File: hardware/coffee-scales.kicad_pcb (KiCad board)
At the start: 2 copper layers, 121.9 x 50.8 mm, 10 parts, among them J1 Conn_01x04, SW1 SW_Push, U1 Adafruit_Feather_328P, U2 HX711_Breakout, U3 4DIGIT_7SEG, U4 4DIGIT_7SEG

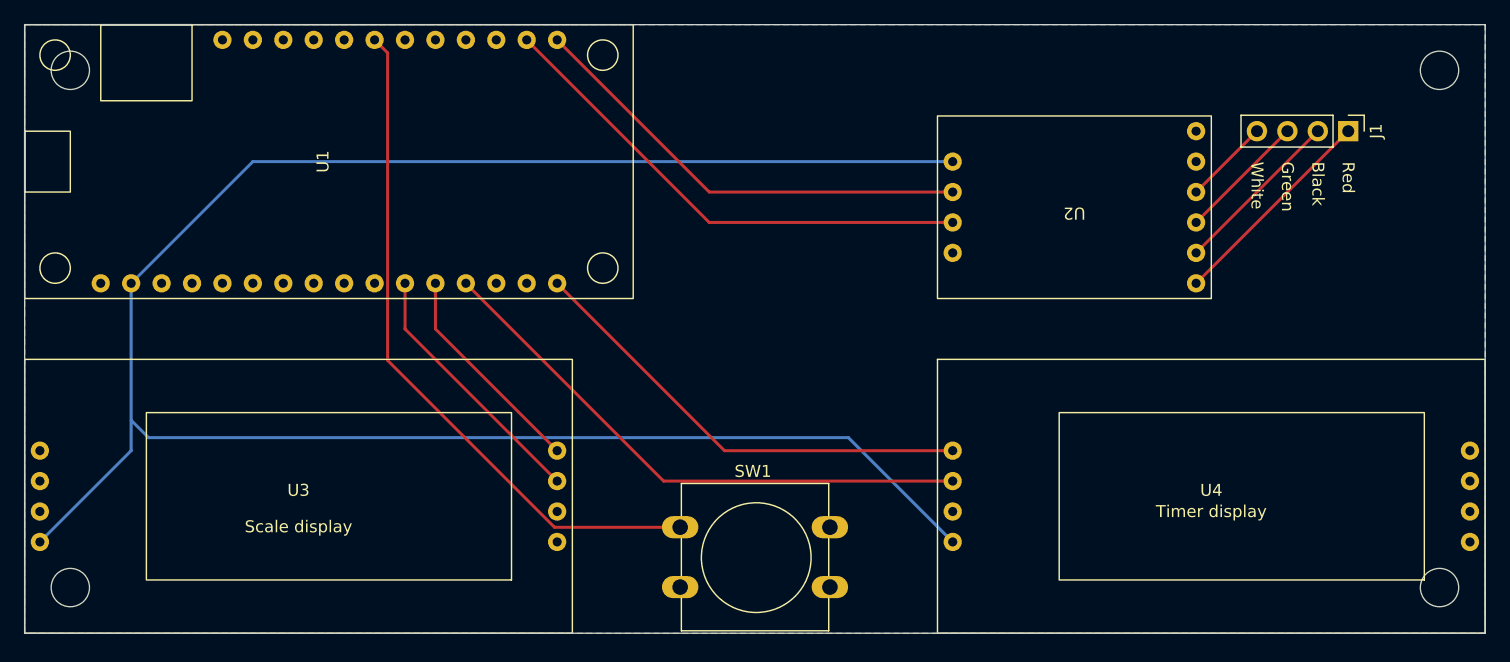
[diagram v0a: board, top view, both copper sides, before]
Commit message: Wire button and HX711 DT to interrupt pins
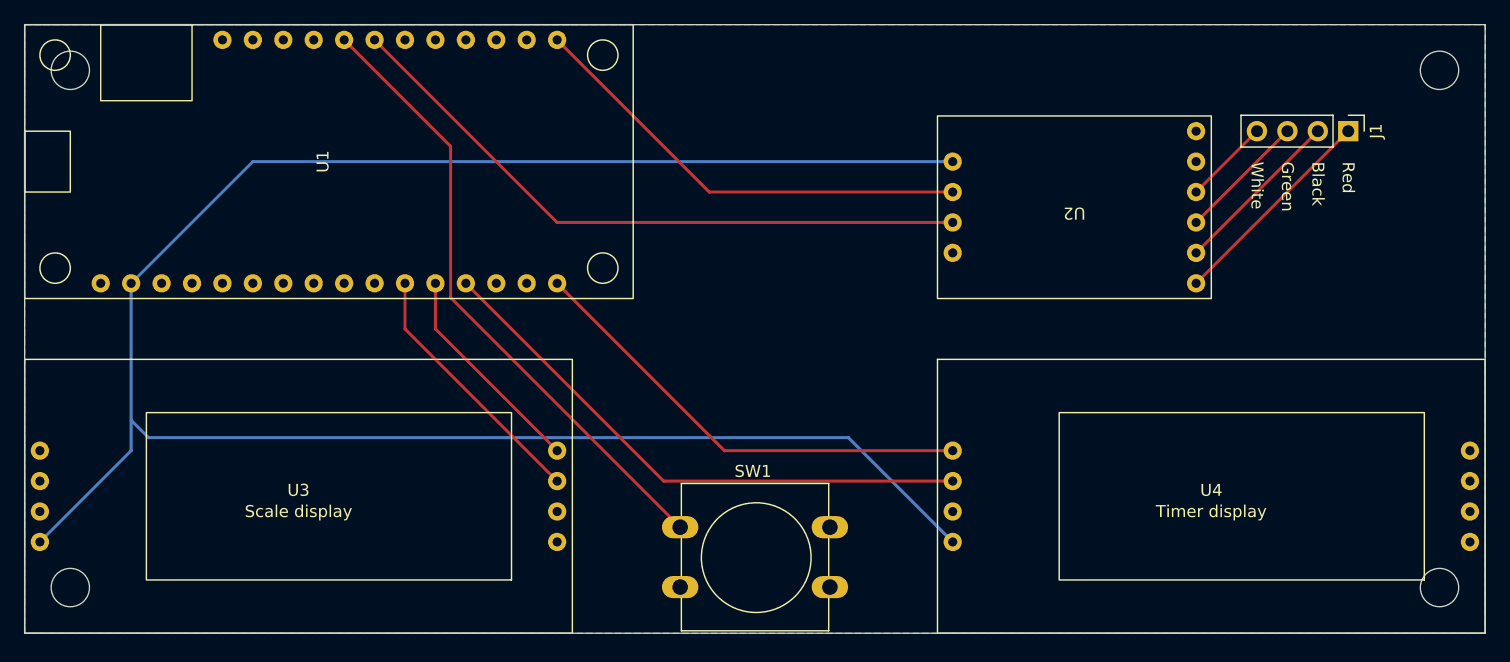
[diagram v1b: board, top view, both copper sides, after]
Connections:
- SW1 pad 1: Net-(U1-Pad22) -> Net-(SW1-Pad1)
- U1 pad 21: unconnected-(U1-Pad21) -> Net-(SW1-Pad1)
- U1 pad 27: Net-(U2-Pad8) -> unconnected-(U1-Pad27)
- U2 pad 8: Net-(U2-Pad8) -> Net-(U1-Pad22)
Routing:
- net Net-(SW1-Pad1): track 0.00 -> 52.3 mm
- net Net-(U2-Pad8): track 41.9 -> 0.00 mm
- net Net-(U1-Pad22): track 57.4 -> 54.6 mm

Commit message: Big but pointless PCB update
* Rounded corners
* Components not so close to the edge
* HX711 data pin on interrupt
* Bigger vias/pads
* Square first pad
* Lots of stuff added to silkscreen

But my gut feeling is the next PCB I have made will be without
all the breakouts anyway.
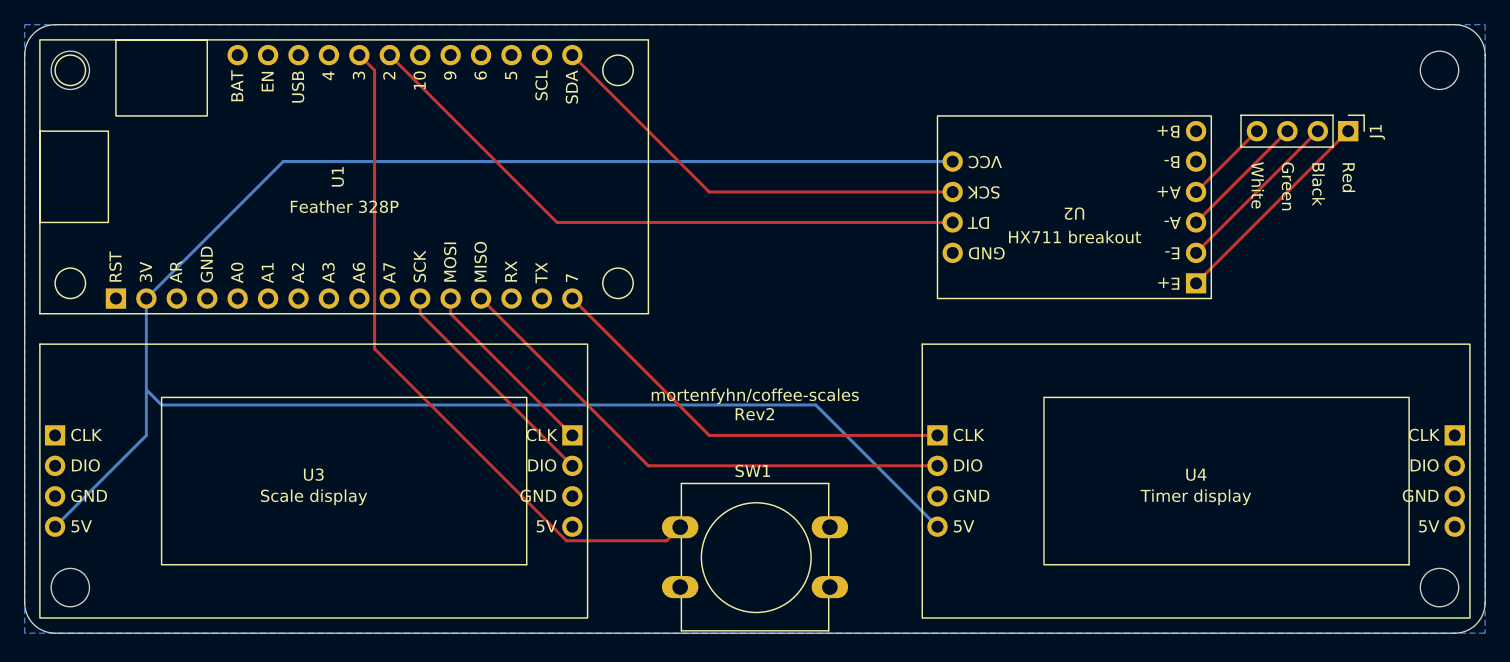
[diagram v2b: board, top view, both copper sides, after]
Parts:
- moved U1 1.80 mm to (59.7, 134.6)
- moved U4 1.80 mm to (130.8, 160.0)
- moved U3 1.80 mm to (57.1, 160.0)
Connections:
- U3 pad 1: Net-(U1-Pad12) -> unconnected-(U3-Pad1)
- U3 pad 2: Net-(U1-Pad11) -> unconnected-(U3-Pad2)
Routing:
- net Net-(SW1-Pad1): track 52.3 -> 57.7 mm
- net +3V3: track 170.3 -> 165.0 mm
- net Net-(U1-Pad13): track 47.5 -> 43.9 mm
- net Net-(U1-Pad16): track 38.8 -> 35.2 mm
- net Net-(U1-Pad11): track 21.8 -> 19.2 mm
- net Net-(U1-Pad12): track 18.2 -> 15.6 mm
- net Net-(U1-Pad22): track 54.6 -> 52.8 mm
- net Net-(U1-Pad28): track 38.3 -> 36.5 mm
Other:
- outline, holes or cut-outs redrawn
- board text added: "Feather 328P"
- board text added: "HX711 breakout"
- board text added: "mortenfyhn/coffee-scales Rev2"

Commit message: Finish HX711 integration
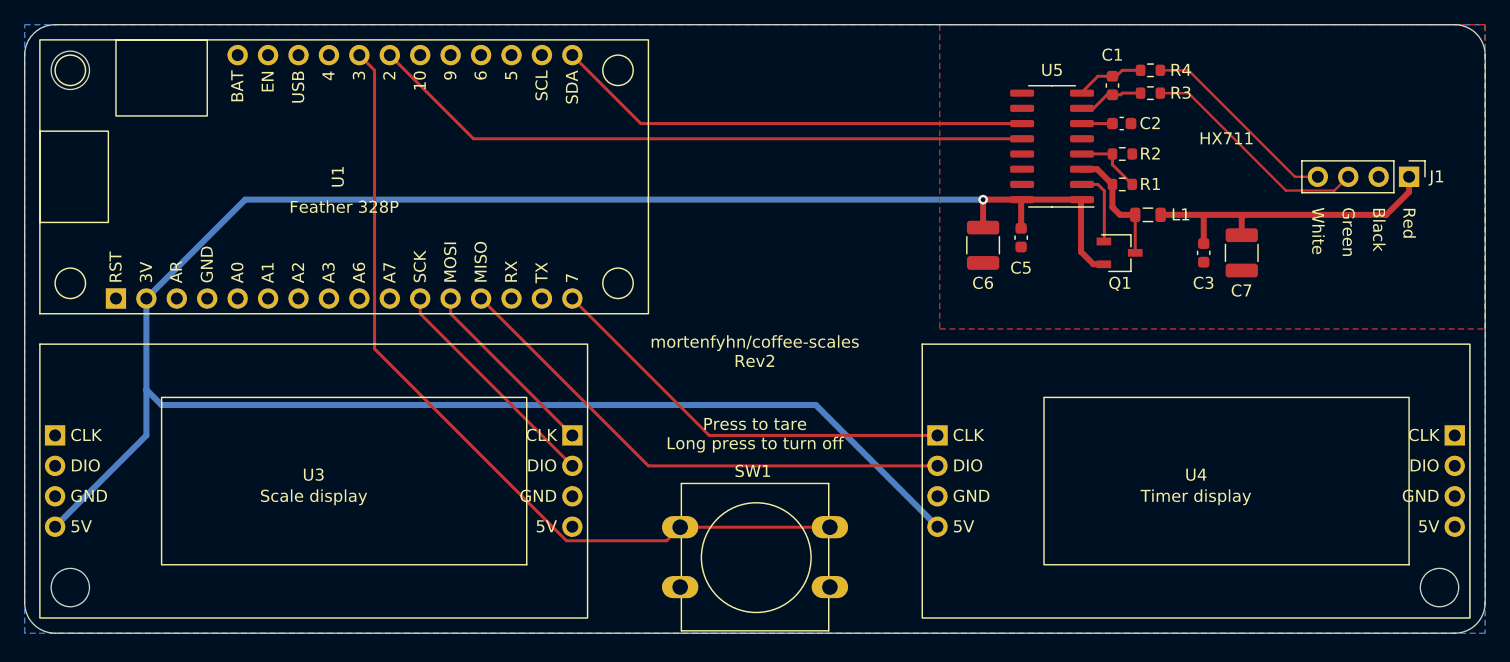
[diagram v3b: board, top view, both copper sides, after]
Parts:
- removed the REF** at (151.1, 125.7)
- removed U2: HX711_Breakout, CoffeeLib:HX711_Breakout
- added C1: 0.1uF, Capacitor_SMD:C_0603_1608Metric, F.Cu at (123.8, 127.0)
- added C2: 0.1uF, Capacitor_SMD:C_0603_1608Metric, F.Cu at (124.6, 130.2)
- added C3: 0.1uF, Capacitor_SMD:C_0603_1608Metric, F.Cu at (131.4, 141.0)
- added C5: 0.1uF, Capacitor_SMD:C_0603_1608Metric, F.Cu at (116.2, 139.7)
- added C6: 10uF, Capacitor_SMD:C_1210_3225Metric, F.Cu at (113.0, 140.3)
- added C7: 10uF, Capacitor_SMD:C_1210_3225Metric, F.Cu at (134.6, 141.0)
- added L1: 3.3uH, Inductor_SMD:L_0805_2012Metric, F.Cu at (126.8, 137.8)
- added Q1: MMBT4403, Package_TO_SOT_SMD:TSOT-23, F.Cu at (124.4, 141.0)
- added R1: 20k, Resistor_SMD:R_0603_1608Metric, F.Cu at (124.7, 135.3)
- added R2: 8.2k, Resistor_SMD:R_0603_1608Metric, F.Cu at (124.7, 132.7)
- added R3: 100, Resistor_SMD:R_0603_1608Metric, F.Cu at (127.0, 127.6)
- added R4: 100, Resistor_SMD:R_0603_1608Metric, F.Cu at (127.0, 125.7)
- added U5: ~, Package_SO:SOP-16_3.9x9.9mm_P1.27mm, F.Cu at (118.8, 132.1)
- moved J1 6.35 mm to (148.6, 134.6)
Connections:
- J1 pad 1: Net-(J1-Pad1) -> /HX711/E+
- J1 pad 2: Net-(J1-Pad2) -> GND
- J1 pad 3: Net-(J1-Pad3) -> /HX711/A-
- J1 pad 4: Net-(J1-Pad4) -> /HX711/A+
- U1 pad 22: Net-(U1-Pad22) -> /HX711/DAT
- U1 pad 28: Net-(U1-Pad28) -> /HX711/SCK
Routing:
- net /HX711/DAT: track 0.00 -> 55.7 mm
- net Net-(U1-Pad22): track 52.8 -> 0.00 mm
- net /HX711/SCK: track 0.00 -> 39.8 mm
- net Net-(U1-Pad28): track 36.5 -> 0.00 mm
- net /HX711/E+: track 0.00 -> 26.8 mm
- net +3V3: track 165.0 -> 186.0 mm, vias 0 -> 1
- net /HX711/A-: track 0.00 -> 19.5 mm
- net Net-(J1-Pad1): track 18.0 -> 0.00 mm
- net /HX711/A+: track 0.00 -> 16.8 mm
- net Net-(J1-Pad2): track 14.4 -> 0.00 mm
- net Net-(U1-D3): track 57.7 -> 70.2 mm
- net Net-(J1-Pad3): track 10.8 -> 0.00 mm
- net Net-(Q1-C): track 0.00 -> 10.4 mm
- net Net-(J1-Pad4): track 7.18 -> 0.00 mm
- net Net-(Q1-B): track 0.00 -> 6.39 mm
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- added copper zone on F.Cu, net GND
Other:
- board text added: "HX711"
- board text added: "Press to tare Long press to turn off"
- board text removed: "HX711 breakout"

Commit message: Route most of the 328 stuff
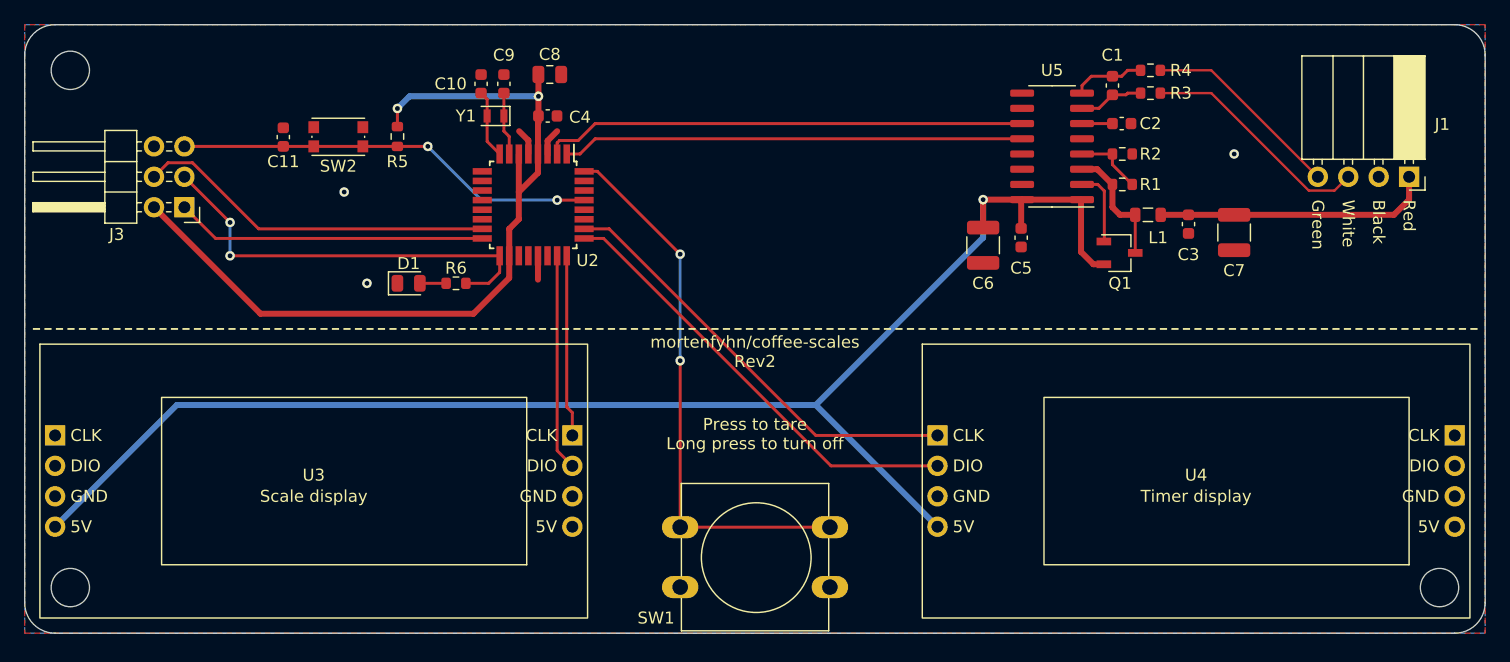
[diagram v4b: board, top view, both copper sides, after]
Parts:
- removed U1: Adafruit_Feather_328P, CoffeeLib:Adafruit_Feather_328P
- added C10: 22pF, Capacitor_SMD:C_0603_1608Metric, F.Cu at (71.1, 126.9)
- added C11: 0.1uF, Capacitor_SMD:C_0603_1608Metric, F.Cu at (54.6, 131.3)
- added C4: 0.1uF, Capacitor_SMD:C_0603_1608Metric, F.Cu at (76.7, 129.5)
- added C8: 10uF, Capacitor_SMD:C_0805_2012Metric, F.Cu at (76.9, 126.1)
- added C9: 22pF, Capacitor_SMD:C_0603_1608Metric, F.Cu at (73.0, 126.9)
- added D1: LED, LED_SMD:LED_0805_2012Metric, F.Cu at (65.1, 143.5)
- added J3: AVR-ISP-6, Connector_PinHeader_2.54mm:PinHeader_2x03_P2.54mm_Horizontal, F.Cu at (46.4, 137.2)
- added R5: 10k, Resistor_SMD:R_0603_1608Metric, F.Cu at (64.1, 131.3)
- added R6: 330, Resistor_SMD:R_0603_1608Metric, F.Cu at (69.0, 143.5)
- added SW2: SW_Push, Button_Switch_SMD:SW_Push_1P1T_NO_CK_KMR2, F.Cu at (59.2, 131.3)
- added U2: ATmega328P-A, Package_QFP:TQFP-32_7x7mm_P0.8mm, F.Cu at (75.5, 137.0)
- added Y1: 8MHz, Crystal:Crystal_SMD_2012-2Pin_2.0x1.2mm, F.Cu at (72.3, 129.5)
- J1: footprint Connector_PinHeader_2.54mm:PinHeader_1x04_P2.54mm_Vertical -> Connector_PinSocket_2.54mm:PinSocket_1x04_P2.54mm_Horizontal
- moved C3 2.72 mm to (130.2, 138.6)
- moved C7 1.81 mm to (134.0, 139.3)
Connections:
- SW1 pad 1: Net-(U1-D3) -> /328P/INT0
- U3 pad 5: Net-(U1-MOSI) -> /328P/GPIO2
- U3 pad 6: Net-(U1-SCK) -> /328P/GPIO1
- U4 pad 1: Net-(U1-D7) -> /328P/GPIO4
- U4 pad 2: Net-(U1-MISO) -> /328P/GPIO3
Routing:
- net Net-(U1-D3): track 70.2 -> 0.00 mm
- net VCC: track 0.00 -> 69.5 mm, vias 0 -> 2
- net +3V3: track 186.0 -> 124.8 mm
- net /328P/INT0: track 0.00 -> 46.3 mm, vias 0 -> 2
- net Net-(U1-MISO): track 43.9 -> 0.00 mm
- net /328P/GPIO3: track 0.00 -> 37.4 mm
- net /328P/GPIO4: track 0.00 -> 36.6 mm
- net /328P/RESET: track 0.00 -> 35.3 mm, vias 0 -> 2
- net /328P/SCK: track 0.00 -> 35.3 mm, vias 0 -> 2
- net Net-(U1-D7): track 35.2 -> 0.00 mm
- net Net-(J3-MOSI): track 0.00 -> 30.2 mm
- net Net-(J3-MISO): track 0.00 -> 25.9 mm
- net Net-(U1-SCK): track 19.2 -> 0.00 mm
- net /328P/GPIO1: track 0.00 -> 18.1 mm
- net /HX711/DAT: track 55.7 -> 38.5 mm
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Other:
- board text removed: "Feather 328P"
- board text removed: "HX711"

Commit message: Create analog ground plane for HX711
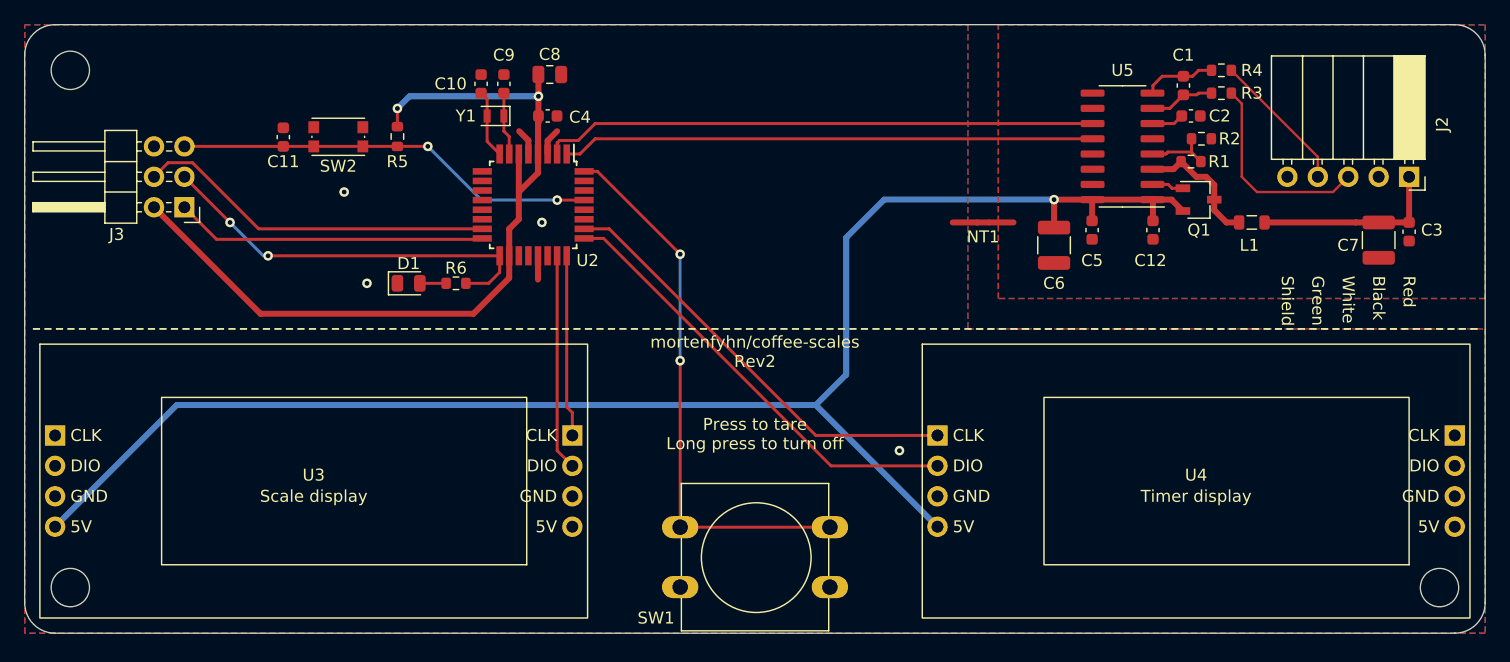
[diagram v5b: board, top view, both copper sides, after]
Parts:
- removed J1: Conn_01x04, Connector_PinSocket_2.54mm:PinSocket_1x04_P2.54mm_Horizontal
- added C12: 0.1uF, Capacitor_SMD:C_0603_1608Metric, F.Cu at (127.2, 139.1)
- added J2: Conn_01x05, Connector_PinSocket_2.54mm:PinSocket_1x05_P2.54mm_Horizontal, F.Cu at (148.6, 134.6)
- added NT1: NetTie_2, NetTie:NetTie-2_SMD_Pad0.5mm, F.Cu at (113.0, 138.4)
- moved C3 18.4 mm to (148.6, 139.2)
- moved C7 12.1 mm to (146.1, 139.9)
- moved L1 8.69 mm to (135.5, 138.4)
- moved Q1 7.96 mm to (131.0, 136.5)
- moved R2 6.73 mm to (131.3, 131.4)
- moved R1 6.04 mm to (130.4, 133.3)
- moved C5 5.96 mm to (122.1, 139.1)
- moved R3 5.92 mm to (132.9, 127.6)
- moved R4 5.92 mm to (132.9, 125.7)
- moved C1 5.92 mm to (129.7, 127.0)
- moved C6 5.92 mm to (119.0, 140.3)
- moved U5 5.88 mm to (124.7, 132.1)
- moved C2 5.82 mm to (130.4, 129.5)
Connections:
- C2 pad 1: GND -> HX_GNDA
- C3 pad 2: GND -> HX_GNDA
- C5 pad 2: GND -> HX_GNDA
- C6 pad 2: GND -> HX_GNDA
- C7 pad 2: GND -> HX_GNDA
- R2 pad 2: GND -> HX_GNDA
- U5 pad 10: GND -> HX_GNDA
- U5 pad 14: GND -> HX_GNDA
- U5 pad 15: GND -> HX_GNDA
- U5 pad 5: GND -> HX_GNDA
- U5 pad 9: GND -> HX_GNDA
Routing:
- net +3V3: track 124.8 -> 132.9 mm
- net /HX711/E+: track 23.2 -> 15.9 mm
- net /HX711/DAT: track 38.5 -> 44.4 mm
- net /HX711/SCK: track 40.4 -> 46.3 mm
- net /HX711/A+: track 16.8 -> 11.9 mm
- net Net-(Q1-B): track 6.39 -> 2.67 mm
- net /HX711/A-: track 19.5 -> 17.3 mm
- net GND: track 6.45 -> 8.49 mm, vias 3 -> 4
- net HX_GNDA: track 0.00 -> 2.04 mm
- net /328P/SCK: track 35.3 -> 33.6 mm
- added copper zone on B.Cu, net HX_GNDA
- added copper zone on F.Cu, net HX_GNDA
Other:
- board text added: "Shield"
